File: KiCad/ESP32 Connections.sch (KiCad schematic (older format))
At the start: 6 parts

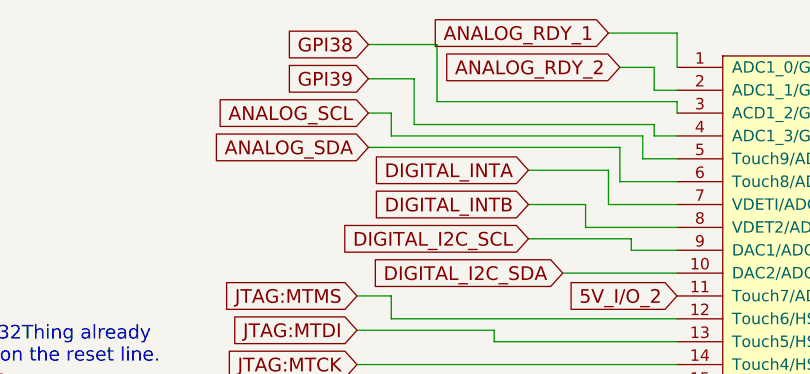
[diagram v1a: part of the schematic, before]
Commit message: Save with sensor inputs using digital potentiometer
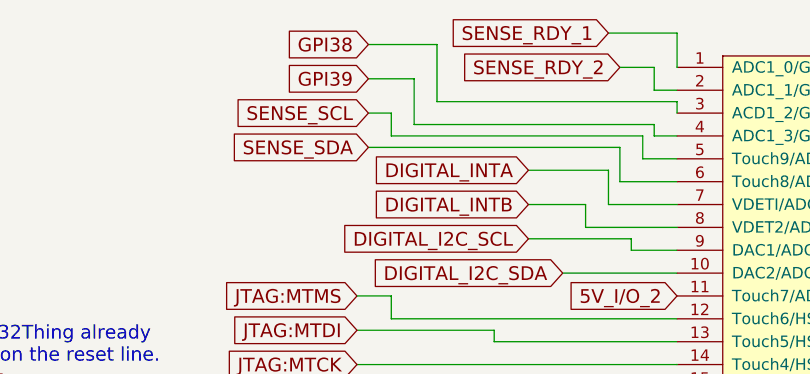
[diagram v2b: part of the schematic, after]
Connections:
- net ANALOG_RDY_1 renamed SENSE_RDY_1
- net ANALOG_RDY_2 renamed SENSE_RDY_2
- net ANALOG_SCL renamed SENSE_SCL
- net ANALOG_SDA renamed SENSE_SDA
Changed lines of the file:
@@
 LIBS:ADS1115IDGST
 LIBS:LM1086
+LIBS:X95840WV20IZ-2_7T1
+LIBS:804-112
 LIBS:HAP-IO-Card-cache
 EELAYER 26 0
@@
 NoConn ~ 5400 4200
 $Comp
-L GND #PWR308
+L GND #PWR058
 U 1 1 5918208C
 P 5200 5900
-F 0 "#PWR308" H 5200 5650 50  0001 C CNN
+F 0 "#PWR058" H 5200 5650 50  0001 C CNN
 F 1 "GND" H 5200 5750 50  0000 C CNN
 F 2 "" H 5200 5900 50  0001 C CNN
@@
 NoConn ~ 5200 3800
 $Comp
-L GND #PWR305
+L GND #PWR059
 U 1 1 59182095
 P 5200 3600
-F 0 "#PWR305" H 5200 3350 50  0001 C CNN
+F 0 "#PWR059" H 5200 3350 50  0001 C CNN
 F 1 "GND" V 5200 3400 50  0000 C CNN
 F 2 "" H 5200 3600 50  0001 C CNN
@@
 $EndComp
 $Comp
-L GND #PWR304
+L GND #PWR060
 U 1 1 5918209B
 P 5150 4300
-F 0 "#PWR304" H 5150 4050 50  0001 C CNN
+F 0 "#PWR060" H 5150 4050 50  0001 C CNN
 F 1 "GND" V 5150 4100 50  0000 C CNN
 F 2 "" H 5150 4300 50  0001 C CNN
@@
 $EndComp
 $Comp
-L GND #PWR306
+L GND #PWR061
 U 1 1 59184108
 P 5200 3900
-F 0 "#PWR306" H 5200 3650 50  0001 C CNN
+F 0 "#PWR061" H 5200 3650 50  0001 C CNN
 F 1 "GND" V 5200 3700 50  0000 C CNN
 F 2 "" H 5200 3900 50  0001 C CNN
@@
 $EndComp
 $Comp
-L GND #PWR307
+L GND #PWR062
 U 1 1 59184116
 P 5200 4000
-F 0 "#PWR307" H 5200 3750 50  0001 C CNN
+F 0 "#PWR062" H 5200 3750 50  0001 C CNN
 F 1 "GND" V 5200 3800 50  0000 C CNN
 F 2 "" H 5200 4000 50  0001 C CNN
@@
 ~RESET
 Text GLabel 3850 2350 0    60   Input ~ 0
-ANALOG_SDA
+SENSE_SDA
 Text GLabel 3850 2200 0    60   Input ~ 0
-ANALOG_SCL
+SENSE_SCL
 Text GLabel 4550 2450 0    60   Input ~ 0
 DIGITAL_INTA
@@
 The Sparkfun ESP32Thing already\nhas a 10k pull-up on the reset line.
 Text GLabel 4900 1850 0    60   Input ~ 0
-ANALOG_RDY_1
+SENSE_RDY_1
 Text GLabel 4950 2000 0    60   Input ~ 0
-ANALOG_RDY_2
+SENSE_RDY_2
 Text GLabel 3450 3950 0    60   Input ~ 0
 POWER3V3
 $Comp
-L +3V3 #PWR303
+L +3V3 #PWR063
 U 1 1 592C50A9
 P 3650 3850
-F 0 "#PWR303" H 3650 3700 50  0001 C CNN
+F 0 "#PWR063" H 3650 3700 50  0001 C CNN
 F 1 "+3V3" V 3665 3978 50  0000 L CNN
 F 2 "" H 3650 3850 50  0001 C CNN
@@
 VSPI_Q/MISO
 $Comp
-L GND #PWR302
+L GND #PWR064
 U 1 1 5924796B
 P 2450 4800
-F 0 "#PWR302" H 2450 4550 50  0001 C CNN
+F 0 "#PWR064" H 2450 4550 50  0001 C CNN
 F 1 "GND" V 2455 4672 50  0000 R CNN
 F 2 "" H 2450 4800 50  0001 C CNN
@@
 $EndComp
 $Comp
-L +3V3 #PWR301
+L +3V3 #PWR065
 U 1 1 5924911C
 P 2200 6050
-F 0 "#PWR301" H 2200 5900 50  0001 C CNN
+F 0 "#PWR065" H 2200 5900 50  0001 C CNN
 F 1 "+3V3" H 2215 6223 50  0000 C CNN
 F 2 "" H 2200 6050 50  0001 C CNN
@@
 	5200 5600 4050 5600
 $Comp
-L PWR_FLAG #FLG301
+L PWR_FLAG #FLG066
 U 1 1 5927191A
 P 4350 3950
-F 0 "#FLG301" H 4350 4025 50  0001 C CNN
+F 0 "#FLG066" H 4350 4025 50  0001 C CNN
 F 1 "PWR_FLAG" V 4350 4078 50  0000 L CNN
 F 2 "" H 4350 3950 50  0001 C CNN

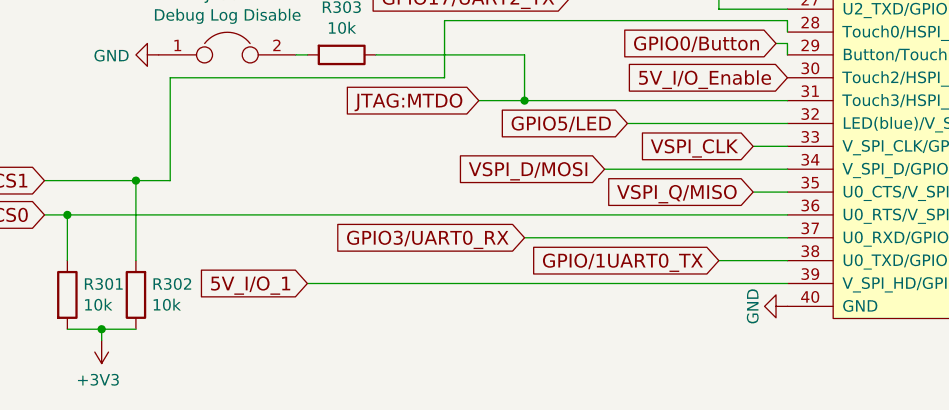
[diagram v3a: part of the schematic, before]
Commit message: Halfway through routing - need better layout to prevent rats nest
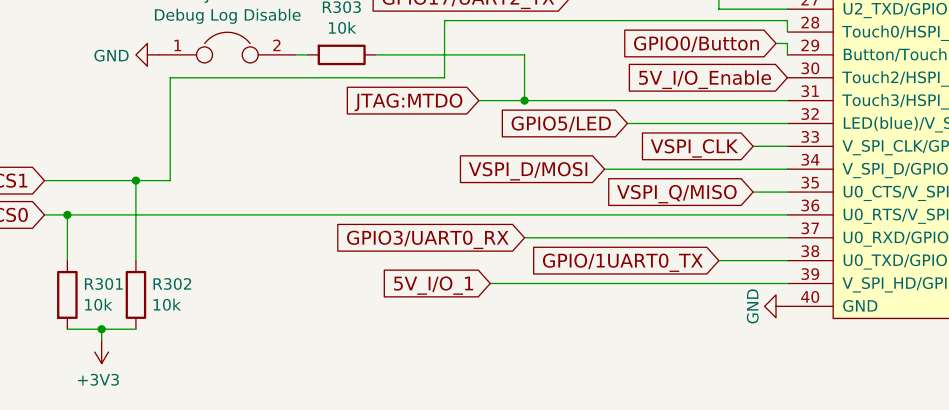
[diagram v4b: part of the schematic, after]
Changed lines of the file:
@@
 NoConn ~ 5400 4200
 $Comp
-L GND #PWR058
+L GND #PWR066
 U 1 1 5918208C
 P 5200 5900
-F 0 "#PWR058" H 5200 5650 50  0001 C CNN
+F 0 "#PWR066" H 5200 5650 50  0001 C CNN
 F 1 "GND" H 5200 5750 50  0000 C CNN
 F 2 "" H 5200 5900 50  0001 C CNN
@@
 NoConn ~ 5200 3800
 $Comp
-L GND #PWR059
+L GND #PWR067
 U 1 1 59182095
 P 5200 3600
-F 0 "#PWR059" H 5200 3350 50  0001 C CNN
+F 0 "#PWR067" H 5200 3350 50  0001 C CNN
 F 1 "GND" V 5200 3400 50  0000 C CNN
 F 2 "" H 5200 3600 50  0001 C CNN
@@
 $EndComp
 $Comp
-L GND #PWR060
+L GND #PWR068
 U 1 1 5918209B
 P 5150 4300
-F 0 "#PWR060" H 5150 4050 50  0001 C CNN
+F 0 "#PWR068" H 5150 4050 50  0001 C CNN
 F 1 "GND" V 5150 4100 50  0000 C CNN
 F 2 "" H 5150 4300 50  0001 C CNN
@@
 $EndComp
 $Comp
-L GND #PWR061
+L GND #PWR069
 U 1 1 59184108
 P 5200 3900
-F 0 "#PWR061" H 5200 3650 50  0001 C CNN
+F 0 "#PWR069" H 5200 3650 50  0001 C CNN
 F 1 "GND" V 5200 3700 50  0000 C CNN
 F 2 "" H 5200 3900 50  0001 C CNN
@@
 $EndComp
 $Comp
-L GND #PWR062
+L GND #PWR070
 U 1 1 59184116
 P 5200 4000
-F 0 "#PWR062" H 5200 3750 50  0001 C CNN
+F 0 "#PWR070" H 5200 3750 50  0001 C CNN
 F 1 "GND" V 5200 3800 50  0000 C CNN
 F 2 "" H 5200 4000 50  0001 C CNN
@@
 POWER3V3
 $Comp
-L +3V3 #PWR063
+L +3V3 #PWR071
 U 1 1 592C50A9
 P 3650 3850
-F 0 "#PWR063" H 3650 3700 50  0001 C CNN
+F 0 "#PWR071" H 3650 3700 50  0001 C CNN
 F 1 "+3V3" V 3665 3978 50  0000 L CNN
 F 2 "" H 3650 3850 50  0001 C CNN
@@
 VSPI_Q/MISO
 $Comp
-L GND #PWR064
+L GND #PWR072
 U 1 1 5924796B
 P 2450 4800
-F 0 "#PWR064" H 2450 4550 50  0001 C CNN
+F 0 "#PWR072" H 2450 4550 50  0001 C CNN
 F 1 "GND" V 2455 4672 50  0000 R CNN
 F 2 "" H 2450 4800 50  0001 C CNN
@@
 $EndComp
 $Comp
-L +3V3 #PWR065
+L +3V3 #PWR073
 U 1 1 5924911C
 P 2200 6050
-F 0 "#PWR065" H 2200 5900 50  0001 C CNN
+F 0 "#PWR073" H 2200 5900 50  0001 C CNN
 F 1 "+3V3" H 2215 6223 50  0000 C CNN
 F 2 "" H 2200 6050 50  0001 C CNN
@@
 	-1   0    0    1
 $EndComp
-Text GLabel 3100 5800 0    60   Input ~ 0
+Text GLabel 3900 5800 0    60   Input ~ 0
 5V_I/O_1
 Wire Wire Line
@@
 $EndComp
 Wire Wire Line
-	3100 5800 5200 5800
+	3900 5800 5200 5800
 Text GLabel 5200 3000 0    60   Input ~ 0
 5V_I/O_2
@@
 	5200 5600 4050 5600
 $Comp
-L PWR_FLAG #FLG066
+L PWR_FLAG #FLG074
 U 1 1 5927191A
 P 4350 3950
-F 0 "#FLG066" H 4350 4025 50  0001 C CNN
+F 0 "#FLG074" H 4350 4025 50  0001 C CNN
 F 1 "PWR_FLAG" V 4350 4078 50  0000 L CNN
 F 2 "" H 4350 3950 50  0001 C CNN

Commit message: Starting another routing pass
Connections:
- net 5V_I/O_1 renamed 5V_IO_1
- net 5V_I/O_2 renamed 5V_IO_2
- net 5V_I/O_Enable renamed 5V_IO_Enable
- net GPIO/1UART0_TX renamed GPIO1/UART0_TX
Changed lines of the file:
@@
 $EndComp
 Text GLabel 3900 5800 0    60   Input ~ 0
-5V_I/O_1
+5V_IO_1
 Wire Wire Line
 	1950 5500 5200 5500
@@
 Connection ~ 4350 3950
 Text GLabel 4900 5700 0    60   Input ~ 0
-GPIO/1UART0_TX
+GPIO1/UART0_TX
 $Comp
 L R R303
@@
 	3900 5800 5200 5800
 Text GLabel 5200 3000 0    60   Input ~ 0
-5V_I/O_2
+5V_IO_2
 Text GLabel 5200 4900 0    60   Input ~ 0
-5V_I/O_Enable
+5V_IO_Enable
 Text GLabel 3850 1900 0    60   Input ~ 0
 GPI38

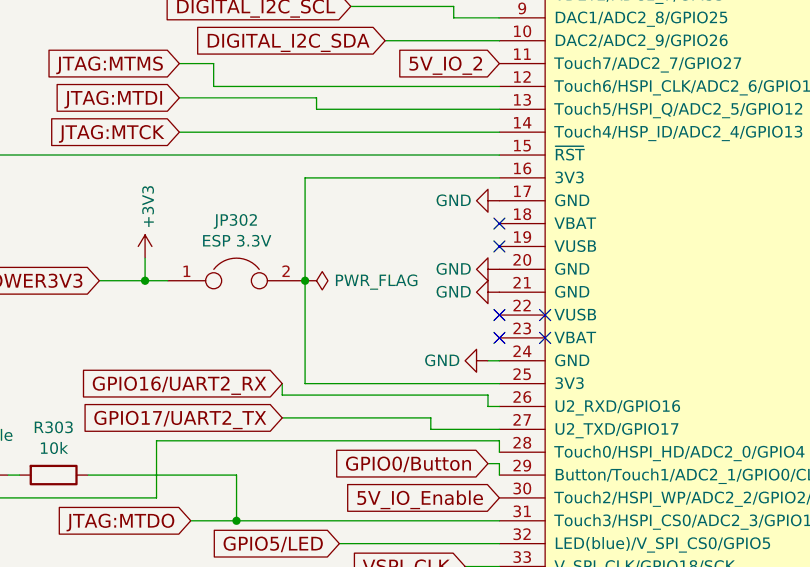
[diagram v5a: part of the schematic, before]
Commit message: Everything routed. ERC Ok
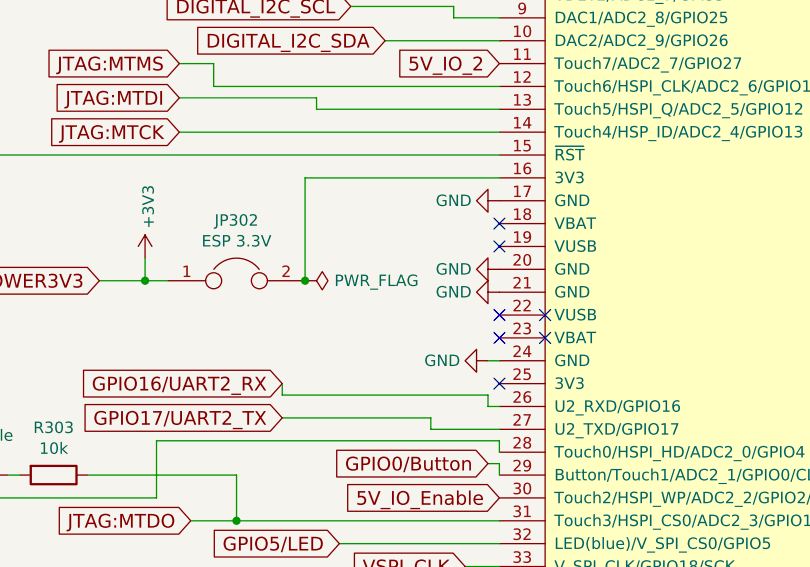
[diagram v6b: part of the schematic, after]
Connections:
- net at JP302.2, SPRKESP301.16 (3V3): no longer SPRKESP301.25 (3V3)
- no-connect marks 6 -> 7
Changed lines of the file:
@@
 Text GLabel 1950 5350 0    60   Input ~ 0
 VSPI_CS1
-Wire Wire Line
-	3800 3300 5200 3300
-Wire Wire Line
-	3800 3150 4400 3150
-Wire Wire Line
-	4400 3150 4400 3200
-Wire Wire Line
-	4400 3200 5200 3200
-Wire Wire Line
-	5200 3100 3950 3100
-Wire Wire Line
-	3950 3100 3950 3000
-Wire Wire Line
-	3950 3000 3800 3000
-Wire Wire Line
-	2300 3400 5200 3400
-Wire Wire Line
-	5200 3500 4350 3500
-Wire Wire Line
-	5050 5200 5200 5200
-Wire Wire Line
-	5050 5400 5200 5400
-Wire Wire Line
-	4700 2900 5200 2900
-Wire Wire Line
-	4550 2750 5000 2750
-Wire Wire Line
-	5000 2750 5000 2800
-Wire Wire Line
-	5000 2800 5200 2800
-Wire Wire Line
-	5200 2700 4800 2700
-Wire Wire Line
-	4800 2700 4800 2600
-Wire Wire Line
-	4800 2600 4550 2600
-Wire Wire Line
-	4550 2450 4900 2450
-Wire Wire Line
-	4900 2450 4900 2600
-Wire Wire Line
-	4900 2600 5200 2600
-Wire Wire Line
-	5200 4300 5150 4300
-Wire Wire Line
-	4950 2000 5100 2000
-Wire Wire Line
-	5100 2000 5100 2100
-Wire Wire Line
-	5100 2100 5200 2100
-Wire Wire Line
-	3650 3950 3650 3850
-Connection ~ 3650 3950
-Wire Wire Line
-	3850 5000 5200 5000
-Wire Wire Line
-	3400 4800 4050 4800
-Wire Wire Line
-	4050 4800 4050 5000
-Connection ~ 4050 5000
-Wire Wire Line
-	4900 5700 5200 5700
-Wire Wire Line
-	3850 2350 4950 2350
-Wire Wire Line
-	4950 2350 4950 2500
-Wire Wire Line
-	4950 2500 5200 2500
-Wire Wire Line
-	3850 2200 3950 2200
-Wire Wire Line
-	3950 2200 3950 2300
-Wire Wire Line
-	3950 2300 5050 2300
-Wire Wire Line
-	5050 2300 5050 2400
-Wire Wire Line
-	5050 2400 5200 2400
-Wire Wire Line
-	4400 5300 5200 5300
 $Comp
 L R R302
@@
 Text GLabel 3900 5800 0    60   Input ~ 0
 5V_IO_1
-Wire Wire Line
-	1950 5500 5200 5500
-Wire Wire Line
-	2050 6000 2350 6000
-Wire Wire Line
-	2200 6000 2200 6050
-Connection ~ 2200 6000
 $Comp
 L Jumper JP302
@@
 	1    0    0    -1
 $EndComp
-Wire Wire Line
-	3450 3950 3750 3950
-Wire Wire Line
-	4350 3500 4350 4400
-Connection ~ 4350 3950
 Text GLabel 4900 5700 0    60   Input ~ 0
 GPIO1/UART0_TX
@@
 	1    0    0    -1
 $EndComp
-Wire Wire Line
-	3900 5800 5200 5800
 Text GLabel 5200 3000 0    60   Input ~ 0
 5V_IO_2
@@
 Text GLabel 3850 2050 0    60   Input ~ 0
 GPI39
-Wire Wire Line
-	5200 2000 5200 1850
-Wire Wire Line
-	5200 1850 4900 1850
-Wire Wire Line
-	3850 1900 4150 1900
-Wire Wire Line
-	4150 1900 4150 2150
-Wire Wire Line
-	4150 2150 5200 2150
-Wire Wire Line
-	5200 2150 5200 2200
-Wire Wire Line
-	3850 2050 4050 2050
-Wire Wire Line
-	4050 2050 4050 2250
-Wire Wire Line
-	4050 2250 5100 2250
-Wire Wire Line
-	5100 2250 5100 2300
-Wire Wire Line
-	5100 2300 5200 2300
-Wire Wire Line
-	4250 4550 4900 4550
-Wire Wire Line
-	4900 4550 4900 4600
-Wire Wire Line
-	4900 4600 5200 4600
-Wire Wire Line
-	4350 4400 5200 4400
-Wire Wire Line
-	5200 4500 5150 4500
-Wire Wire Line
-	5150 4500 5150 4450
-Wire Wire Line
-	5150 4450 4250 4450
-Wire Wire Line
-	4250 4450 4250 4400
 Text GLabel 5150 4750 0    60   Input ~ 0
 GPIO0/Button
-Wire Wire Line
-	5150 4750 5200 4750
-Wire Wire Line
-	5200 4750 5200 4800
 Text GLabel 4500 5100 0    60   Input ~ 0
 GPIO5/LED
-Wire Wire Line
-	4500 5100 5200 5100
 Text GLabel 4250 4400 0    60   Input ~ 0
 GPIO16/UART2_RX
 Text GLabel 4250 4550 0    60   Input ~ 0
 GPIO17/UART2_TX
-Wire Wire Line
-	2050 5700 2050 5500
-Connection ~ 2050 5500
-Wire Wire Line
-	5200 4700 5200 4650
-Wire Wire Line
-	5200 4650 3700 4650
-Wire Wire Line
-	3700 4650 3700 4900
-Wire Wire Line
-	3700 4900 2500 4900
-Wire Wire Line
-	2500 4900 2500 5350
-Wire Wire Line
-	2500 5350 1950 5350
-Wire Wire Line
-	2350 5700 2350 5350
-Connection ~ 2350 5350
 Text GLabel 4050 5600 0    60   Input ~ 0
 GPIO3/UART0_RX
-Wire Wire Line
-	3100 4800 3050 4800
-Wire Wire Line
-	5200 5600 4050 5600
 $Comp
 L PWR_FLAG #FLG074
@@
 	0    1    1    0
 $EndComp
+Wire Wire Line
+	3800 3300 5200 3300
+Wire Wire Line
+	3800 3150 4400 3150
+Wire Wire Line
+	4400 3150 4400 3200
+Wire Wire Line
+	4400 3200 5200 3200
+Wire Wire Line
+	5200 3100 3950 3100
+Wire Wire Line
+	3950 3100 3950 3000
+Wire Wire Line
+	3950 3000 3800 3000
+Wire Wire Line
+	2300 3400 5200 3400
+Wire Wire Line
+	5050 5200 5200 5200
+Wire Wire Line
+	5050 5400 5200 5400
+Wire Wire Line
+	4700 2900 5200 2900
+Wire Wire Line
+	4550 2750 5000 2750
+Wire Wire Line
+	5000 2750 5000 2800
+Wire Wire Line
+	5000 2800 5200 2800
+Wire Wire Line
+	5200 2700 4800 2700
+Wire Wire Line
+	4800 2700 4800 2600
+Wire Wire Line
+	4800 2600 4550 2600
+Wire Wire Line
+	4550 2450 4900 2450
+Wire Wire Line
+	4900 2450 4900 2600
+Wire Wire Line
+	4900 2600 5200 2600
+Wire Wire Line
+	5200 4300 5150 4300
+Wire Wire Line
+	4950 2000 5100 2000
+Wire Wire Line
+	5100 2000 5100 2100
+Wire Wire Line
+	5100 2100 5200 2100
+Wire Wire Line
+	3650 3950 3650 3850
+Connection ~ 3650 3950
+Wire Wire Line
+	3850 5000 5200 5000
+Wire Wire Line
+	3400 4800 4050 4800
+Wire Wire Line
+	4050 4800 4050 5000
+Connection ~ 4050 5000
+Wire Wire Line
+	4900 5700 5200 5700
+Wire Wire Line
+	3850 2350 4950 2350
+Wire Wire Line
+	4950 2350 4950 2500
+Wire Wire Line
+	4950 2500 5200 2500
+Wire Wire Line
+	3850 2200 3950 2200
+Wire Wire Line
+	3950 2200 3950 2300
+Wire Wire Line
+	3950 2300 5050 2300
+Wire Wire Line
+	5050 2300 5050 2400
+Wire Wire Line
+	5050 2400 5200 2400
+Wire Wire Line
+	4400 5300 5200 5300
+Wire Wire Line
+	1950 5500 5200 5500
+Wire Wire Line
+	2050 6000 2350 6000
+Wire Wire Line
+	2200 6000 2200 6050
+Connection ~ 2200 6000
+Wire Wire Line
+	3450 3950 3750 3950
+Connection ~ 4350 3950
+Wire Wire Line
+	3900 5800 5200 5800
+Wire Wire Line
+	5200 2000 5200 1850
+Wire Wire Line
+	5200 1850 4900 1850
+Wire Wire Line
+	3850 1900 4150 1900
+Wire Wire Line
+	4150 1900 4150 2150
+Wire Wire Line
+	4150 2150 5200 2150
+Wire Wire Line
+	5200 2150 5200 2200
+Wire Wire Line
+	3850 2050 4050 2050
+Wire Wire Line
+	4050 2050 4050 2250
+Wire Wire Line
+	4050 2250 5100 2250
+Wire Wire Line
+	5100 2250 5100 2300
+Wire Wire Line
+	5100 2300 5200 2300
+Wire Wire Line
+	4250 4550 4900 4550
+Wire Wire Line
+	4900 4550 4900 4600
+Wire Wire Line
+	4900 4600 5200 4600
+Wire Wire Line
+	5200 4500 5150 4500
+Wire Wire Line
+	5150 4500 5150 4450
+Wire Wire Line
+	5150 4450 4250 4450
+Wire Wire Line
+	4250 4450 4250 4400
+Wire Wire Line
+	5150 4750 5200 4750
+Wire Wire Line
+	5200 4750 5200 4800
+Wire Wire Line
+	4500 5100 5200 5100
+Wire Wire Line
+	2050 5700 2050 5500
+Connection ~ 2050 5500
+Wire Wire Line
+	5200 4700 5200 4650
+Wire Wire Line
+	5200 4650 3700 4650
+Wire Wire Line
+	3700 4650 3700 4900
+Wire Wire Line
+	3700 4900 2500 4900
+Wire Wire Line
+	2500 4900 2500 5350
+Wire Wire Line
+	2500 5350 1950 5350
+Wire Wire Line
+	2350 5700 2350 5350
+Connection ~ 2350 5350
+Wire Wire Line
+	3100 4800 3050 4800
+Wire Wire Line
+	5200 5600 4050 5600
+NoConn ~ 5200 4400
+Wire Wire Line
+	5200 3500 4350 3500
+Wire Wire Line
+	4350 3500 4350 3950
 $EndSCHEMATC

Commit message: Increased ground plane coverage
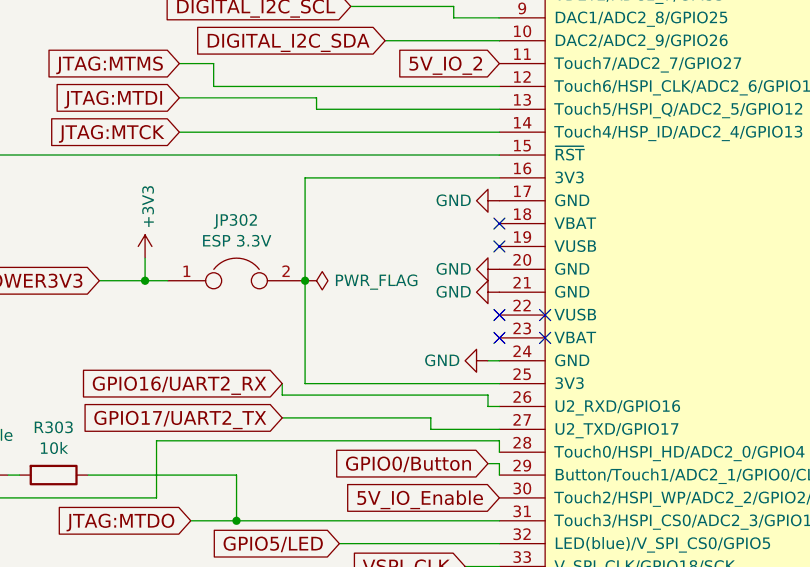
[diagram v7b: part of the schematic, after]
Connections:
- net at JP302.2, SPRKESP301.16 (3V3): now also SPRKESP301.25 (3V3)
- no-connect marks 7 -> 6
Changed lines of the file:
@@
 Wire Wire Line
 	5200 5600 4050 5600
-NoConn ~ 5200 4400
 Wire Wire Line
 	5200 3500 4350 3500
 Wire Wire Line
-	4350 3500 4350 3950
+	4350 3500 4350 4400
+Wire Wire Line
+	4350 4400 5200 4400
 $EndSCHEMATC
